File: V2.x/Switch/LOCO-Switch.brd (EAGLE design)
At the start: 43.2 x 34.3 mm, 55 parts, among them IC1 Atmega 328-P, IC2 MCP2515, IC3 ACS712ELCTR-20A-T, IC5 LM340MP-05, J1 3-794618-4, J2 3-794618-4, Q1 8MHz, Q2 16MHz, Q3 FDS5680, Q4 FDS5680, Q5 FDS5680, Q6 FDS5680, Q7 FDS5680, Q8 FDS5680, X1 22-23-2081

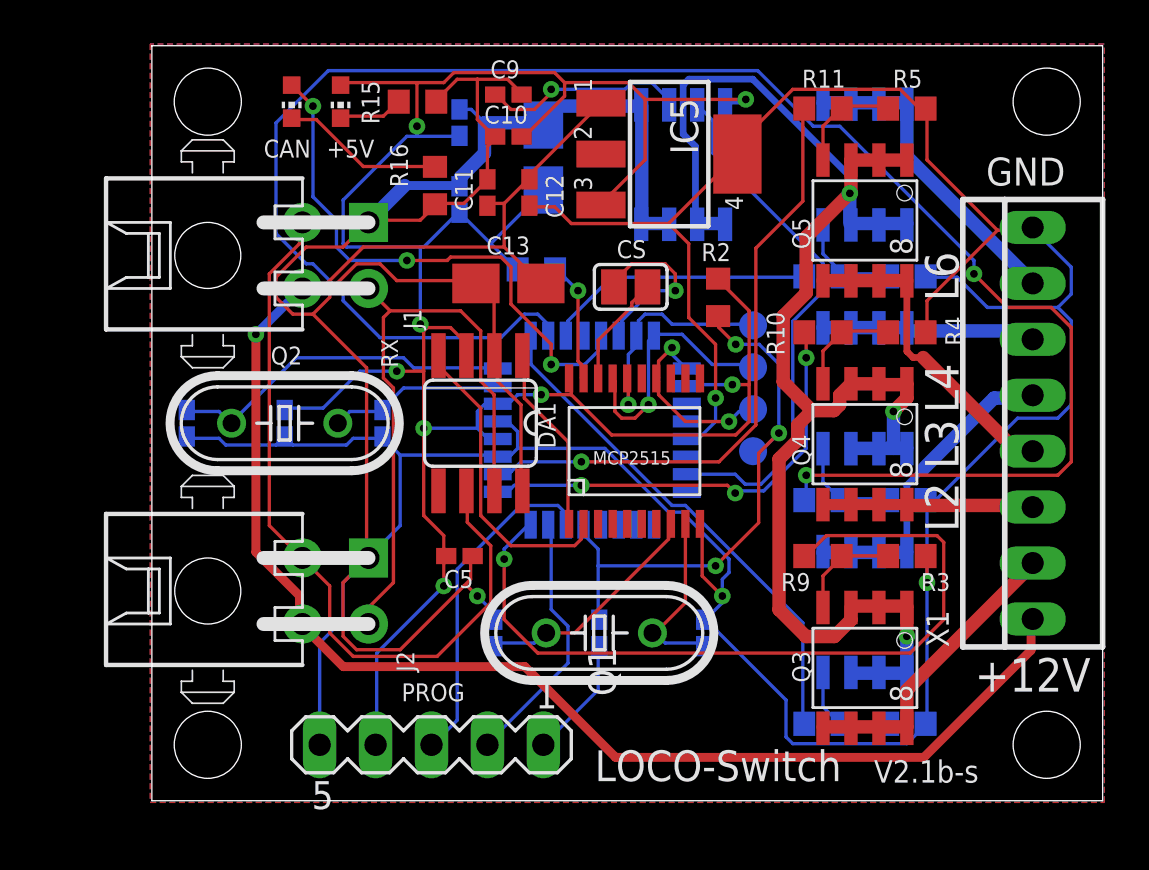
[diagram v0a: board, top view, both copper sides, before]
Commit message: added Loco-CAN icon to motor, servo and switch boards
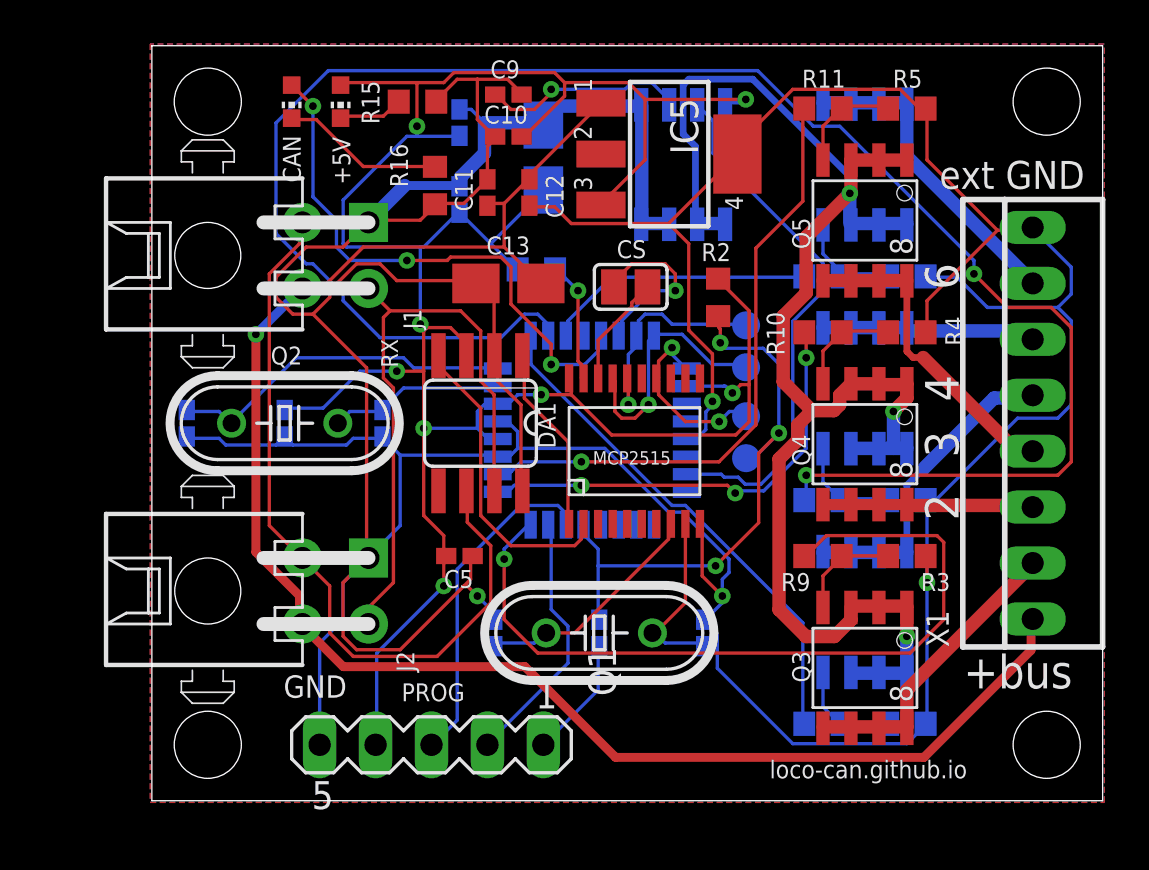
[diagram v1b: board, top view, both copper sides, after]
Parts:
- removed SK, SK1: PTR1B1,27, testpad:B1,27
- added RS, SC: PTR1B1,27, testpad:B1,27
- moved SI 0.32 mm to (27.0, 19.7)
- moved SO 0.32 mm to (27.0, 21.6)
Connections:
- net MCU_RESET: now also RS.TP; no longer SK1.TP
- net SCK: now also SC.TP; no longer SK.TP
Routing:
- net MCU_RESET: track 25.8 -> 26.6 mm
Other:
- board text added: "+bus"
- board text added: "2"
- board text added: "3"
- board text added: "4"
- board text added: "6"
- board text added: "C:/Users/Tom/Nextcloud/Technik/Projekte/Eisenbahn/Gartenbahn/Loco-CAN/Loco-CAN-Hardware/Graphics/Loco-can Logo.bmp"
- board text added: "C:/Users/Tom/Nextcloud/Technik/Projekte/Eisenbahn/Gartenbahn/Loco-CAN/Loco-CAN-Hardware/Graphics/oshw.bmp"
- board text added: "ICP"
- board text added: "Switch"
- board text added: "V2.2"
- board text added: "ext GND"
- board text added: "loco-can.github.io"
- board text removed: "+12V"
- board text removed: "L2"
- board text removed: "L3"
- board text removed: "L4"
- board text removed: "L6"
- board text removed: "LOCO-Switch"
- board text removed: "V2.1b-s"

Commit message: design clean up
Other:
- board text removed: "RX"

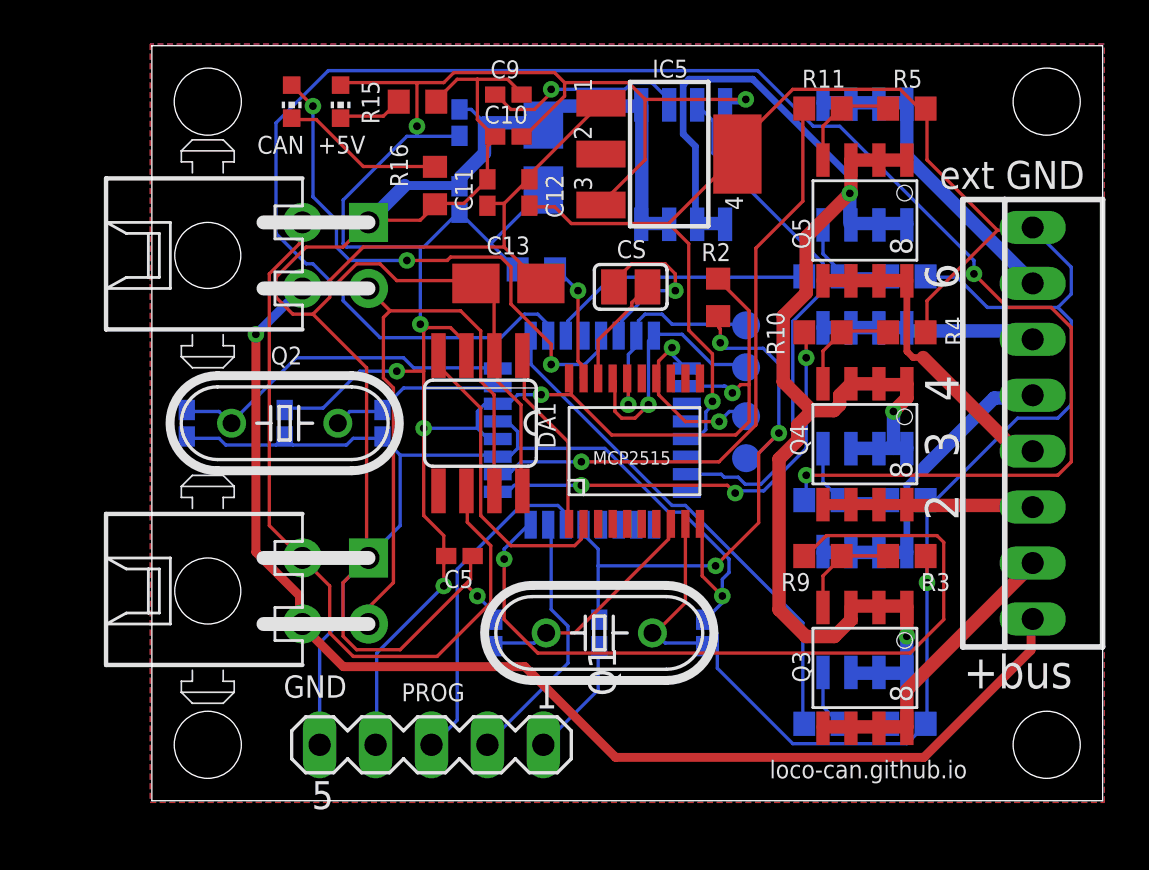
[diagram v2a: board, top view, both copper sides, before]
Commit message: changed sch and brd of motor and switch for RX/TX leds
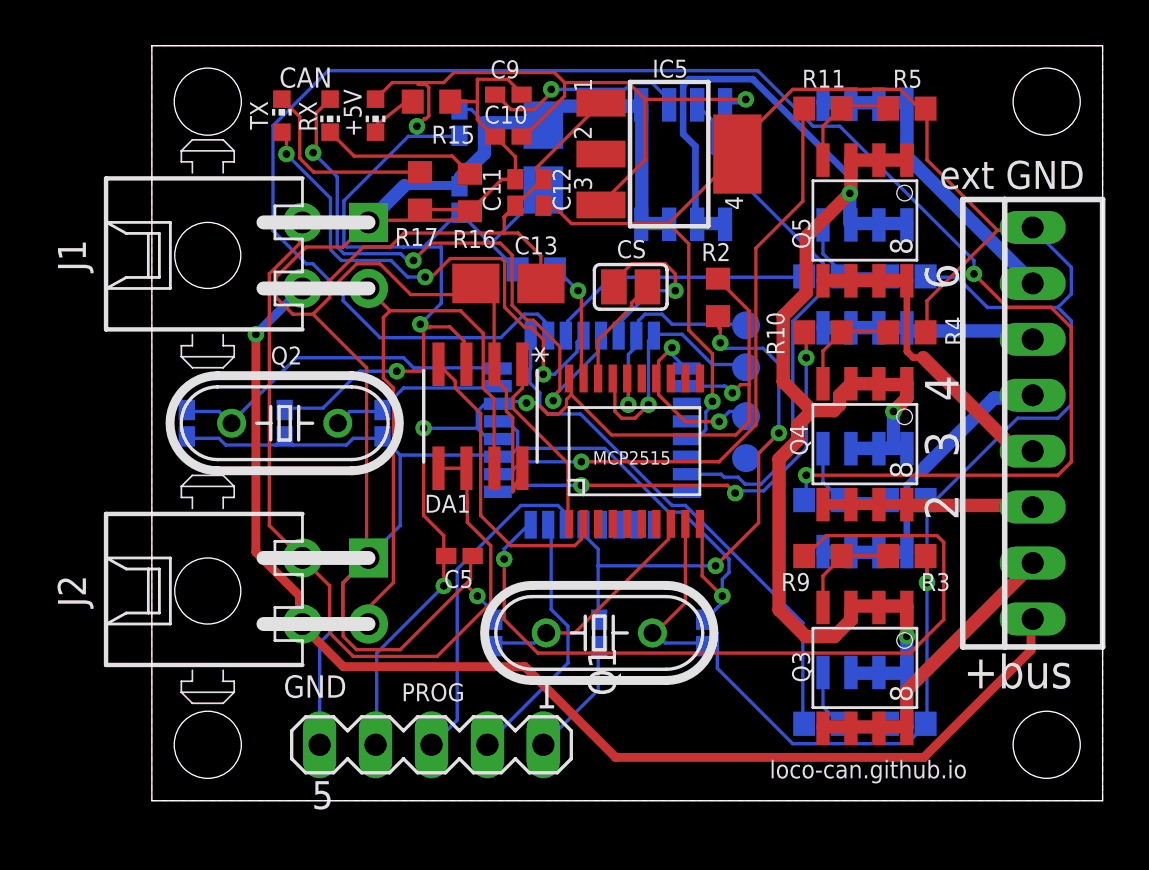
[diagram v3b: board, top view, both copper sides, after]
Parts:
- removed CAN: GRN, led:CHIP-LED0603
- added R17: 33R, rcl:R0603
- added RX: RD, led:CHIP-LED0603
- added TX: WRT, led:CHIP-LED0603
- DA1: value TJA1050 -> MCP2551-X/SNSOIC8-N_MC_MCH; device TJA1050:SO08 -> MCP2551:SOIC8-N_MC_MCH
- IC2: device mcp2514:TSSOP20 -> MCP2515:TSSOP20
- J1, J2: device SamacSys_Parts:SHDRRA4W102P300_2X2_686X892X73 -> Micro Mate-N-Lok:3-794618-4
- PROG: device con-lstb:MA05-1 -> lst-b:MA05-1
- R16: value 10k -> 33R
- moved +5V 1.71 mm to (10.2, 31.1)
- moved R16 1.62 mm to (14.4, 27.6)
- moved C11 1.27 mm to (16.5, 27.6)
- moved C12 0.64 mm to (17.8, 27.6)
- moved R15 0.63 mm to (12.7, 31.8)
- moved DA1 0.32 mm to (14.9, 17.5), turned to 270 degrees
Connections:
- new net D8: IC1.12, TX.A
- new net N$13: R17.1, TX.C
- net CAN-L: now also DA1.5
- net D9: now also RX.A; no longer CAN.A
- net GND: now also R17.2
- net N$9: now also RX.C; no longer CAN.C
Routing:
- net D8: track 0.00 -> 23.9 mm, vias 0 -> 3
- net N$13: track 0.00 -> 8.74 mm
- net GND: track 242.2 -> 245.8 mm
- net D9: track 25.0 -> 27.9 mm
- net CAN-L: track 34.8 -> 37.0 mm
- net VCC: track 116.6 -> 118.2 mm
- net D5: track 23.2 -> 24.1 mm
- net CAN-H: track 28.4 -> 29.3 mm
- net +12V: track 77.8 -> 78.4 mm
- net N$12: track 2.94 -> 2.33 mm
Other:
- board text added: "CAN"
